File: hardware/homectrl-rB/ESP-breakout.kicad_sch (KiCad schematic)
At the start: 26 parts, among them J2 USB_C_Female_USB2_Small, SW1 SW_RESET, SW2 SW_BOOT, U1 ESP32-S3-WROOM-1

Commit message: more routing work
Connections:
- net GPIO_15 is gone; now on net S3-RX: U1.8 (IO15)
- net GPIO_16 is gone; now on net ENN: U1.9 (IO16)
- net ADC-RDY: no longer U1.4 (IO4)
- net DIR: now also U1.6 (IO6); no longer U1.20 (IO12)
- net ENN: no longer U1.21 (IO13)
- net PGATE-0: now also U1.10 (IO17); no longer U1.17 (IO9)
- net PGATE-1: now also U1.11 (IO18); no longer U1.18 (IO10)
- net S3-RX: no longer U1.11 (IO18)
- net S3-TX: now also U1.7 (IO7); no longer U1.10 (IO17)
- net SGATE-0: no longer U1.7 (IO7)
- net STEP: now also U1.5 (IO5); no longer U1.19 (IO11)
- net GPIO_41: now reaches U1.34 (IO41)
- net GPIO_41: now also R8.1
- net GPIO_42: now reaches U1.35 (IO42)
- net GPIO_42: now also R7.1
- removed net GPIO_05: R7.1, U1.5 (IO5)
- removed net GPIO_06: R8.1, U1.6 (IO6)
- new net GPIO_09: U1.17 (IO9)
- new net GPIO_10: U1.18 (IO10)
- new net GPIO_11: U1.19 (IO11)
- new net GPIO_12: U1.20 (IO12)
- new net GPIO_13: U1.21 (IO13)
- no-connect marks 13 -> 12

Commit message: more more routing routing work work
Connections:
- net GPIO_11 is gone; now on net ADC-RDY: U1.19 (IO11)
- net GPIO_12 is gone; now on net SGATE-1: U1.20 (IO12)
- net GPIO_13 is gone; now on net SGATE-0: U1.21 (IO13)

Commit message: W
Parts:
- C13, C14, C15, C16, C35, C36, C37, D14, D7, D8, D9, J2, U1: Purchase (none) -> Yes
- R10, R11, R28, R29, R30, R7, R8, R9, SW1, SW2, TP1, TP2, TP3: Purchase (none) -> N/A

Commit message: add new caps, add ferrite bead, add MPNs
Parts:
- D7: MPN (none) -> COM-24837
- J2: MPN (none) -> USB4105-GF-A-120
- R10, R11, R28, R29, R30, R7, R8, R9: Purchase N/A -> Yes
- SW1, SW2: MPN (none) -> 1825910-6
- TP1, TP2, TP3: MPN (none) -> N/A
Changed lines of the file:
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@@
 			)
 		)
-		(property "Purchase" "N/A"
+		(property "Purchase" "Yes"
 			(at 254 59.69 0)
 			(effects
@@
 			)
 		)
-		(property "Purchase" "N/A"
+		(property "Purchase" "Yes"
 			(at 40.64 83.82 0)
 			(effects
@@
 			)
 		)
-		(property "MPN" ""
+		(property "MPN" "N/A"
 			(at 233.68 55.88 0)
 			(effects
@@
 			)
 		)
-		(property "Purchase" "N/A"
+		(property "Purchase" "Yes"
 			(at 233.68 59.69 0)
 			(effects
@@
 			)
 		)
-		(property "Datasheet" "~"
+		(property "Datasheet" "https://www.te.com/commerce/DocumentDelivery/DDEController?Action=srchrtrv&DocNm=Tactile_Switches&DocType=Data%20Sheet&DocLang=English&DocFormat=pdf&PartCntxt=1825910-6"
 			(at 77.47 50.8 0)
 			(effects
@@
 			)
 		)
-		(property "MPN" ""
+		(property "MPN" "1825910-6"
 			(at 77.47 55.88 0)
 			(effects
@@
 			)
 		)
-		(property "Purchase" "N/A"
+		(property "Purchase" "Yes"
 			(at 237.49 78.74 0)
 			(effects
@@
 			)
 		)
-		(property "MPN" ""
+		(property "MPN" "COM-24837"
 			(at 49.53 124.46 0)
 			(effects
@@
 			)
 		)
-		(property "MPN" ""
+		(property "MPN" "N/A"
 			(at 181.61 68.58 0)
 			(effects
@@
 			)
 		)
-		(property "MPN" ""
+		(property "MPN" "USB4105-GF-A-120"
 			(at 214.63 72.39 0)
 			(effects
@@
 			)
 		)
-		(property "Datasheet" "~"
+		(property "Datasheet" "https://www.te.com/commerce/DocumentDelivery/DDEController?Action=srchrtrv&DocNm=Tactile_Switches&DocType=Data%20Sheet&DocLang=English&DocFormat=pdf&PartCntxt=1825910-6"
 			(at 44.45 50.8 0)
 			(effects
@@
 			)
 		)
-		(property "MPN" ""
+		(property "MPN" "1825910-6"
 			(at 44.45 55.88 0)
 			(effects
@@
 			)
 		)
-		(property "Purchase" "N/A"
+		(property "Purchase" "Yes"
 			(at 233.68 62.23 0)
 			(effects
@@
 			)
 		)
-		(property "Purchase" "N/A"
+		(property "Purchase" "Yes"
 			(at 121.92 64.77 0)
 			(effects
@@
 			)
 		)
-		(property "MPN" ""
+		(property "MPN" "N/A"
 			(at 173.99 68.58 0)
 			(effects
@@
 			)
 		)
-		(property "Purchase" "N/A"
+		(property "Purchase" "Yes"
 			(at 33.02 120.65 0)
 			(effects
@@
 			)
 		)
-		(property "Purchase" "N/A"
+		(property "Purchase" "Yes"
 			(at 59.69 83.82 0)
 			(effects

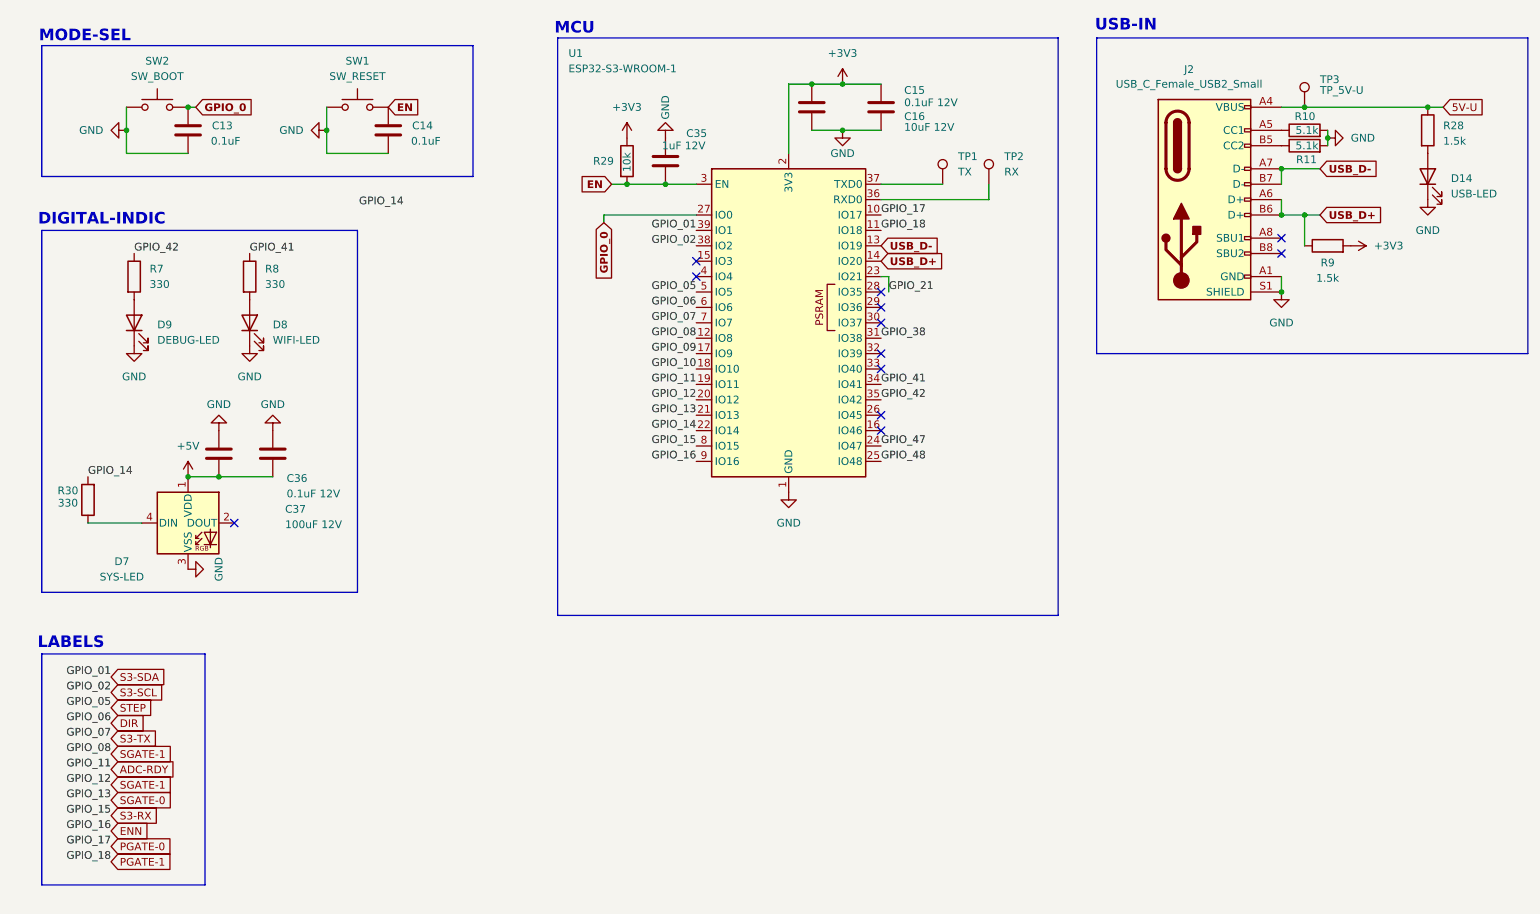
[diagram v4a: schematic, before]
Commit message: add MPNs and review circuits
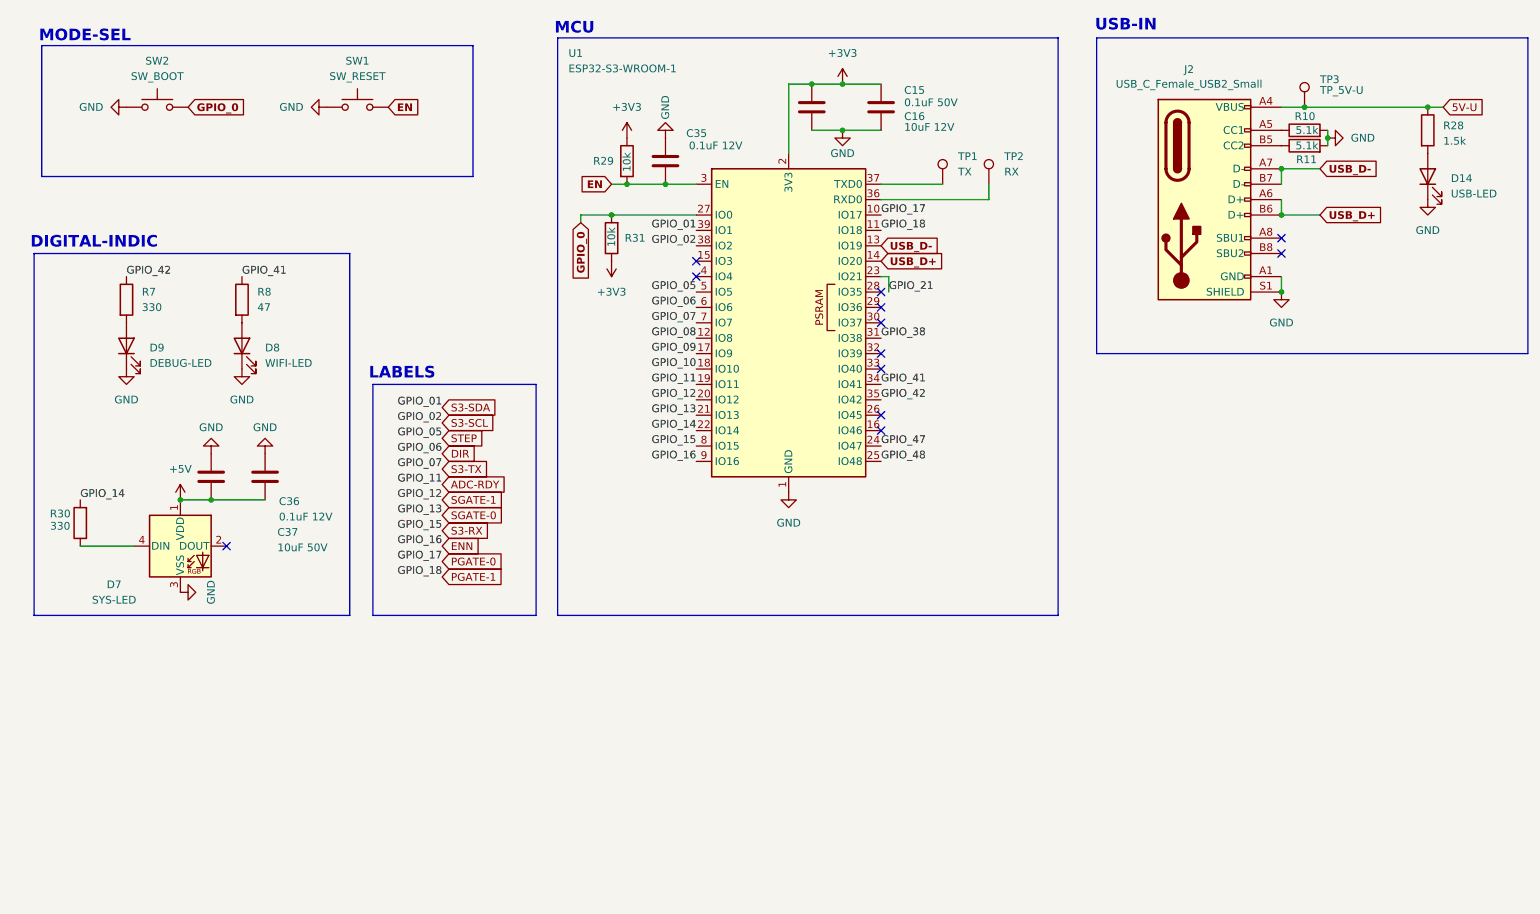
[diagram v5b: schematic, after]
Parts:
- removed C13, C14: 0.1uF, Capacitor_SMD:C_0603_1608Metric, symbol Device:C
- removed R9: 1.5k, Resistor_SMD:R_0402_1005Metric, symbol Device:R
- added R31: 10k, Resistor_SMD:R_0402_1005Metric, symbol Device:R
- C15: value 0.1uF 12V -> 0.1uF 50V; MPN (none) -> GRM155R71H104KE14D
- C16: MPN (none) -> CL10X106MO8NRNC
- C35: value 1uF 12V -> 0.1uF 12V; MPN (none) -> GRM188R71H104KA93D
- C36: MPN (none) -> GRM155R71H104KE14D
- C37: value 100uF 12V -> 10uF 50V; MPN (none) -> CL31A106KBHNNNE
- D14: MPN (none) -> 150060GS75000
- D8: MPN (none) -> 150080BS75000
- D9: MPN (none) -> 150080RS75000
- R10, R11: MPN (none) -> ERJ-3EKF5101V
- R28: MPN (none) -> ERJ-2RKF1501X
- R29: MPN (none) -> ERJ-2RKF1002X
- R30, R7: MPN (none) -> ERJ-2GEJ331X
- R8: value 330 -> 47; MPN (none) -> ERJ-2GEJ331X
- U1: MPN (none) -> ESP32-S3-WROOM-1-N16R8
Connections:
- net +3V3: now also R31.1
- net GPIO_0: now also R31.2
- net SGATE-1: no longer U1.12 (IO8)
- new net GPIO_08: U1.12 (IO8)
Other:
- moved on the sheet: C36, C37, D7, D8, D9, R30, R7, R8

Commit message: pad clearance & BOM fixes
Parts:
- C15: MPN GRM155R71H104KE14D -> CC0603KRX7R9BB104
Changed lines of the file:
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@@
 			)
 		)
-		(property "MPN" "GRM155R71H104KE14D"
+		(property "MPN" "CC0603KRX7R9BB104"
 			(at 152.4 55.88 0)
 			(effects

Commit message: swap connector in progress
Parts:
- C15: value 0.1uF 50V -> 0.1uF
- C16: value 10uF 12V -> 10uF
- C35, C36: value 0.1uF 12V -> 0.1uF
- C37: value 10uF 50V -> 10uF
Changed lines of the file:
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@@
 			)
 		)
+		(property "Comments" ""
+			(at 254 59.69 0)
+			(effects
+				(font
+					(size 1.27 1.27)
+				)
+				(hide yes)
+			)
+		)
 		(pin "2"
 		)
@@
 			)
 		)
-		(property "Value" "10uF 12V"
+		(property "Value" "10uF "
 			(at 167.64 59.1819 0)
 			(effects
@@
 			)
 		)
+		(property "Comments" ""
+			(at 163.83 55.88 0)
+			(effects
+				(font
+					(size 1.27 1.27)
+				)
+				(hide yes)
+			)
+		)
 		(pin "2"
 		)
@@
 			)
 		)
+		(property "Comments" ""
+			(at 39.37 87.63 0)
+			(effects
+				(font
+					(size 1.27 1.27)
+				)
+				(hide yes)
+			)
+		)
 		(pin "1"
 		)
@@
 			)
 		)
+		(property "Comments" ""
+			(at 233.68 55.88 0)
+			(effects
+				(font
+					(size 1.27 1.27)
+				)
+				(hide yes)
+			)
+		)
 		(pin "1"
 		)
@@
 			)
 		)
-		(property "Value" "0.1uF 12V"
+		(property "Value" "0.1uF "
 			(at 64.516 123.444 0)
 			(effects
@@
 			)
 		)
+		(property "Comments" ""
+			(at 62.23 116.84 0)
+			(effects
+				(font
+					(size 1.27 1.27)
+				)
+				(hide yes)
+			)
+		)
 		(pin "2"
 		)
@@
 			)
 		)
+		(property "Comments" ""
+			(at 233.68 59.69 0)
+			(effects
+				(font
+					(size 1.27 1.27)
+				)
+				(hide yes)
+			)
+		)
 		(pin "2"
 		)
@@
 			)
 		)
+		(property "Comments" ""
+			(at 254 67.31 0)
+			(effects
+				(font
+					(size 1.27 1.27)
+				)
+				(hide yes)
+			)
+		)
 		(pin "1"
 		)
@@
 			)
 		)
-		(property "Value" "0.1uF 12V"
+		(property "Value" "0.1uF "
 			(at 140.97 62.23 0)
 			(effects
@@
 			)
 		)
+		(property "Comments" ""
+			(at 128.27 64.77 0)
+			(effects
+				(font
+					(size 1.27 1.27)
+				)
+				(hide yes)
+			)
+		)
 		(pin "2"
 		)
@@
 			)
 		)
+		(property "Comments" ""
+			(at 58.42 95.25 0)
+			(effects
+				(font
+					(size 1.27 1.27)
+				)
+				(hide yes)
+			)
+		)
 		(pin "2"
 		)
@@
 			)
 		)
+		(property "Comments" ""
+			(at 77.47 55.88 0)
+			(effects
+				(font
+					(size 1.27 1.27)
+				)
+				(hide yes)
+			)
+		)
 		(pin "2"
 		)
@@
 			)
 		)
+		(property "Comments" ""
+			(at 48.26 128.27 0)
+			(effects
+				(font
+					(size 1.27 1.27)
+				)
+				(hide yes)
+			)
+		)
 		(pin "1"
 		)
@@
 			)
 		)
-		(property "Value" "0.1uF 50V"
+		(property "Value" "0.1uF"
 			(at 167.64 55.1181 0)
 			(effects
@@
 			)
 		)
+		(property "Comments" ""
+			(at 152.4 55.88 0)
+			(effects
+				(font
+					(size 1.27 1.27)
+				)
+				(hide yes)
+			)
+		)
 		(pin "2"
 		)
@@
 			)
 		)
+		(property "Comments" ""
+			(at 181.61 68.58 0)
+			(effects
+				(font
+					(size 1.27 1.27)
+				)
+				(hide yes)
+			)
+		)
 		(pin "1"
 		)
@@
 			)
 		)
+		(property "Comments" ""
+			(at 119.38 77.47 0)
+			(effects
+				(font
+					(size 1.27 1.27)
+				)
+				(hide yes)
+			)
+		)
 		(pin "2"
 		)
@@
 			)
 		)
+		(property "Comments" ""
+			(at 214.63 72.39 0)
+			(effects
+				(font
+					(size 1.27 1.27)
+				)
+				(hide yes)
+			)
+		)
 		(pin "A1"
 		)
@@
 			)
 		)
+		(property "Comments" ""
+			(at 39.37 95.25 0)
+			(effects
+				(font
+					(size 1.27 1.27)
+				)
+				(hide yes)
+			)
+		)
 		(pin "2"
 		)
@@
 			)
 		)
+		(property "Comments" ""
+			(at 44.45 55.88 0)
+			(effects
+				(font
+					(size 1.27 1.27)
+				)
+				(hide yes)
+			)
+		)
 		(pin "2"
 		)
@@
 			)
 		)
+		(property "Comments" ""
+			(at 233.68 62.23 0)
+			(effects
+				(font
+					(size 1.27 1.27)
+				)
+				(hide yes)
+			)
+		)
 		(pin "2"
 		)
@@
 			)
 		)
+		(property "Comments" ""
+			(at 148.59 91.44 0)
+			(effects
+				(font
+					(size 1.27 1.27)
+				)
+				(hide yes)
+			)
+		)
 		(pin "14"
 		)
@@
 			)
 		)
+		(property "Comments" ""
+			(at 121.92 64.77 0)
+			(effects
+				(font
+					(size 1.27 1.27)
+				)
+				(hide yes)
+			)
+		)
 		(pin "2"
 		)
@@
 			)
 		)
+		(property "Comments" ""
+			(at 173.99 68.58 0)
+			(effects
+				(font
+					(size 1.27 1.27)
+				)
+				(hide yes)
+			)
+		)
 		(pin "1"
 		)
@@
 			)
 		)
-		(property "Value" "10uF 50V"
+		(property "Value" "10uF "
 			(at 64.262 128.524 0)
 			(effects
@@
 			)
 		)
+		(property "Comments" ""
+			(at 53.34 116.84 0)
+			(effects
+				(font
+					(size 1.27 1.27)
+				)
+				(hide yes)
+			)
+		)
 		(pin "2"
 		)
@@
 			)
 		)
+		(property "Comments" ""
+			(at 31.75 124.46 0)
+			(effects
+				(font
+					(size 1.27 1.27)
+				)
+				(hide yes)
+			)
+		)
 		(pin "1"
 		)
@@
 			(at 58.42 87.63 0)
 			(effects
+				(font
+					(size 1.27 1.27)
+				)
+				(hide yes)
+			)
+		)
+		(property "Comments" ""
+			(at 58.42 87.63 0)
+			(effects

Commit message: dssadasdas
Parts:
- D9: Comments (none) -> Brand: Wurth Elektronik
- U1: Comments (none) -> Confirmed part number is ESP32-S3-WROOM-1-n16R8, different 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
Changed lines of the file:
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@@
 			)
 		)
-		(property "Comments" ""
+		(property "Comments" "Brand: Wurth Elektronik"
 			(at 39.37 95.25 0)
 			(effects
@@
 			)
 		)
-		(property "Comments" ""
-			(at 148.59 91.44 0)
-			(effects
+		(property "Comments" "Confirmed part number is ESP32-S3-WROOM-1-n16R8, different from, not WROOM-1-n16R2"
+			(at 148.59 91.44 0)
+			(effects
